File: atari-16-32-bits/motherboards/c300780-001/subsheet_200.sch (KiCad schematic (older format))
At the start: 21 parts, among them J200 DIN5 — MIDI OUT, J201 DIN5 — MIDI IN, U200 MC6850_PHY, U208 PC900_PHY, U210 7406_PHY

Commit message: Use real t filter symbol
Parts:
- removed L200, L201, L202, L204, L205, L206: T_FILTER_2PINS, symbol misc:T_FILTER_2PINS
- added L200, L201, L202, L204, L205, L206: EMI_Filter_LCL, symbol Device:EMI_Filter_LCL
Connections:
- net labels added: in_4, in_4_filtered, in_5_filtered, out_1, out_3, out_4, out_5
- wire segments 79 -> 81
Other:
- note removed: "T Filters"
- moved on the sheet: D202, J200, J201, R200, R202, R204, R205, U208

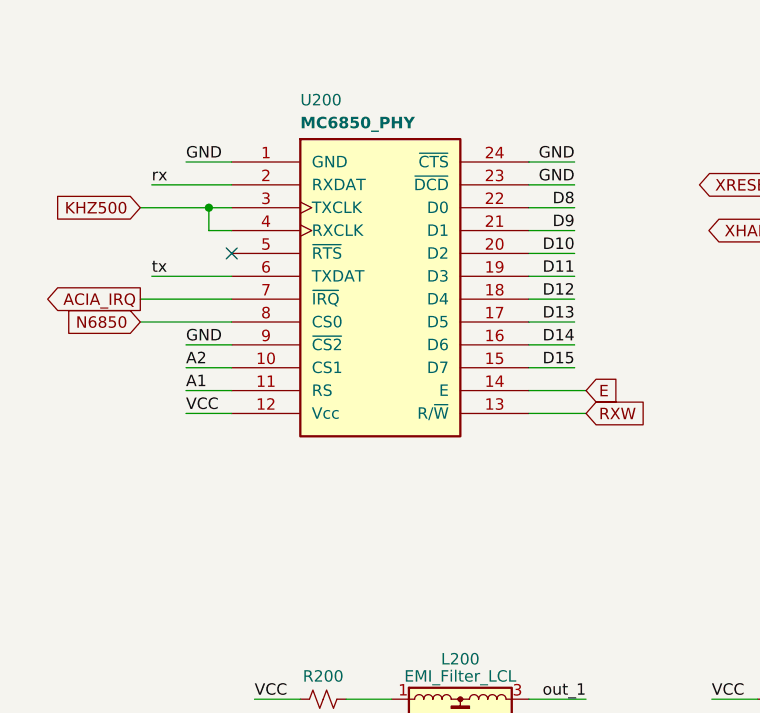
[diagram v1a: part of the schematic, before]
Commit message: done acia2 and ikbd
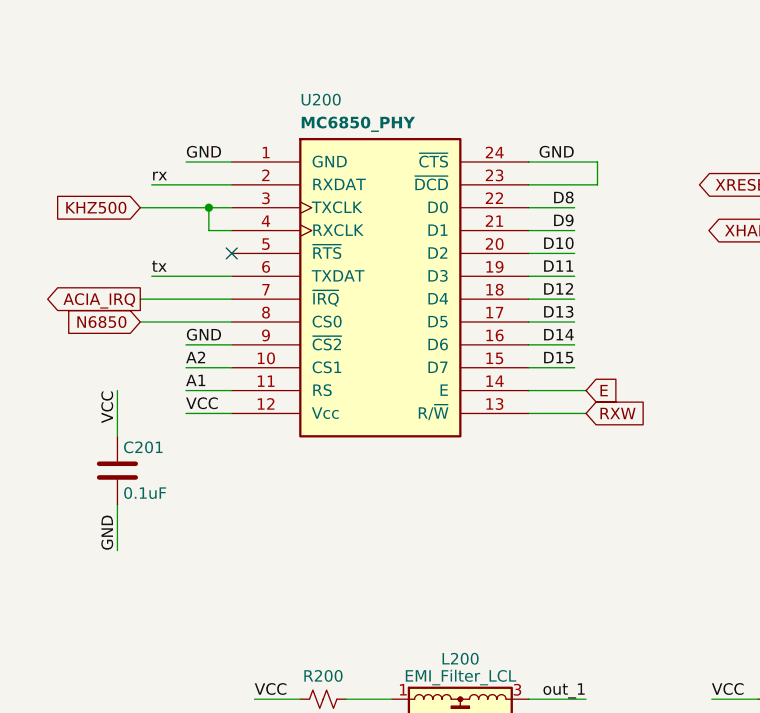
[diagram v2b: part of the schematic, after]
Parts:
- added C201: 0.1uF, symbol Device:C
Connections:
- net GND: now also C201.2
- net VCC: now also C201.1
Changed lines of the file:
@@
 $Descr A4 8268 11693 portrait
 encoding utf-8
-Sheet 9 9
+Sheet 9 10
 Title ""
 Date ""
@@
 VCC
 Text Label 3250 1900 2    50   ~ 0
-GND
-Text Label 3250 2000 2    50   ~ 0
 GND
 NoConn ~ 1750 2300
@@
 	1550 3000 1750 3000
 Wire Wire Line
-	3050 1900 3250 1900
-Wire Wire Line
-	3050 2000 3250 2000
-Wire Wire Line
 	3050 2100 3250 2100
 Wire Wire Line
@@
 Wire Wire Line
 	3000 6200 3500 6200
+$Comp
+L Device:C C?
+U 1 1 608CAEAC
+P 1250 3250
+AR Path="/60786F27/6078774E/608CAEAC" Ref="C?"  Part="1"
+AR Path="/60786F27/607875AF/608CAEAC" Ref="C?"  Part="1"
+AR Path="/6089D0BA/608CAEAC" Ref="C?"  Part="1"
+AR Path="/608A2359/608CAEAC" Ref="C201"  Part="1"
+F 0 "C201" H 1275 3350 50  0000 L CNN
+F 1 "0.1uF" H 1275 3150 50  0000 L CNN
+F 2 "" H 1288 3100 50  0001 C CNN
+F 3 "~" H 1250 3250 50  0001 C CNN
+	1    1250 3250
+	1    0    0    -1
+$EndComp
+Text Label 1250 3600 1    50   ~ 0
+GND
+Text Label 1250 2900 3    50   ~ 0
+VCC
+Wire Wire Line
+	1250 2900 1250 3100
+Wire Wire Line
+	1250 3400 1250 3600
+Wire Wire Line
+	3050 1900 3350 1900
+Wire Wire Line
+	3050 2000 3350 2000
+Wire Wire Line
+	3350 2000 3350 1900
 $EndSCHEMATC
